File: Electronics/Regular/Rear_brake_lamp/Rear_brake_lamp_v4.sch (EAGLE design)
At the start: 8 parts, among them X2 JST-XH-02-PIN-LONG-PAD

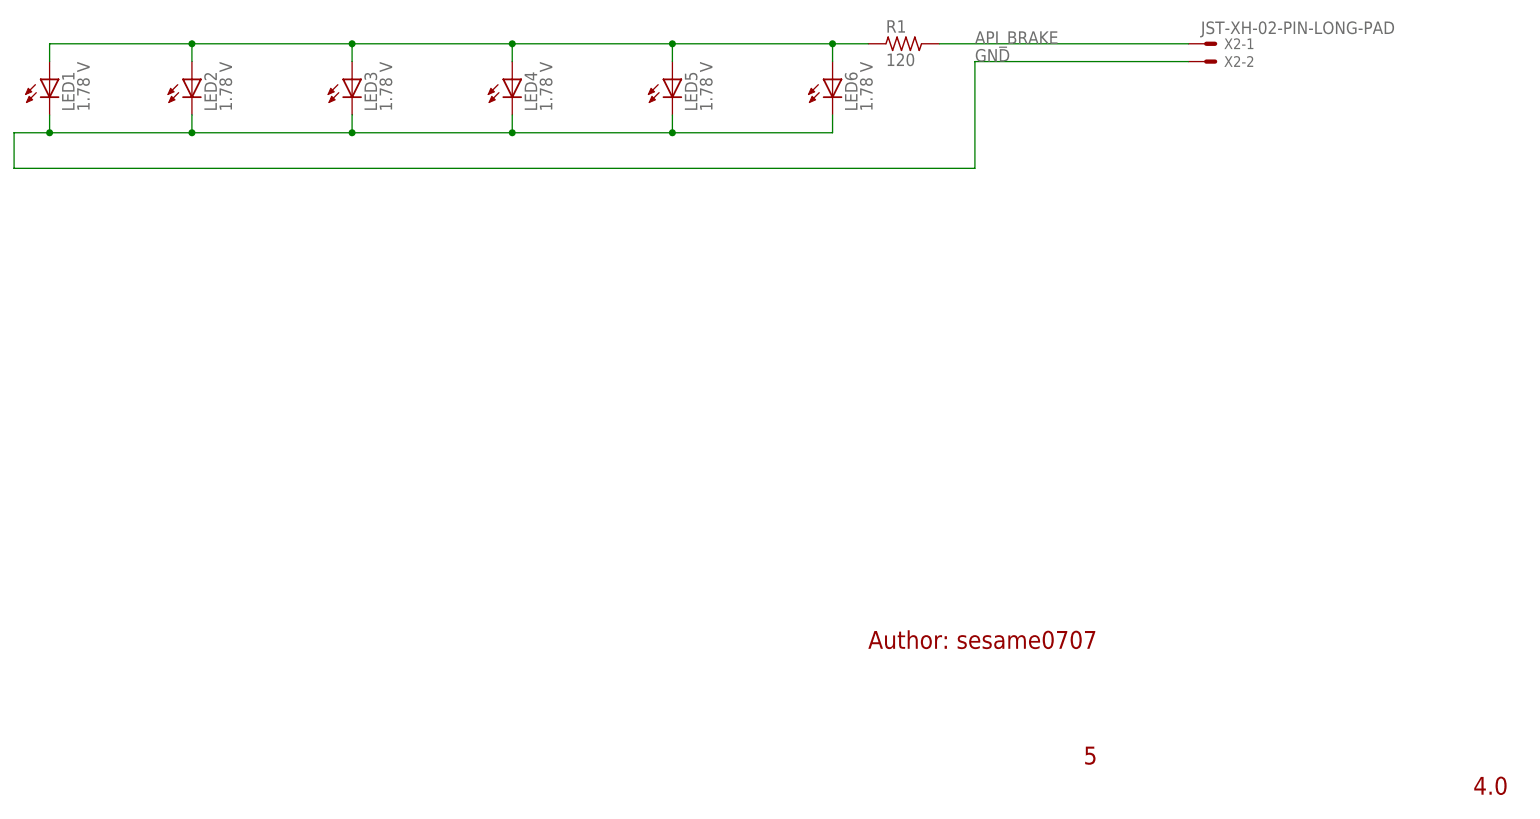
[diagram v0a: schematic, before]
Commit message: BOM on all the lamps added
Note: Version of lamps' projects has increased from x.0 to x.1.

What also has been done:
- some visual refactoring on schematics
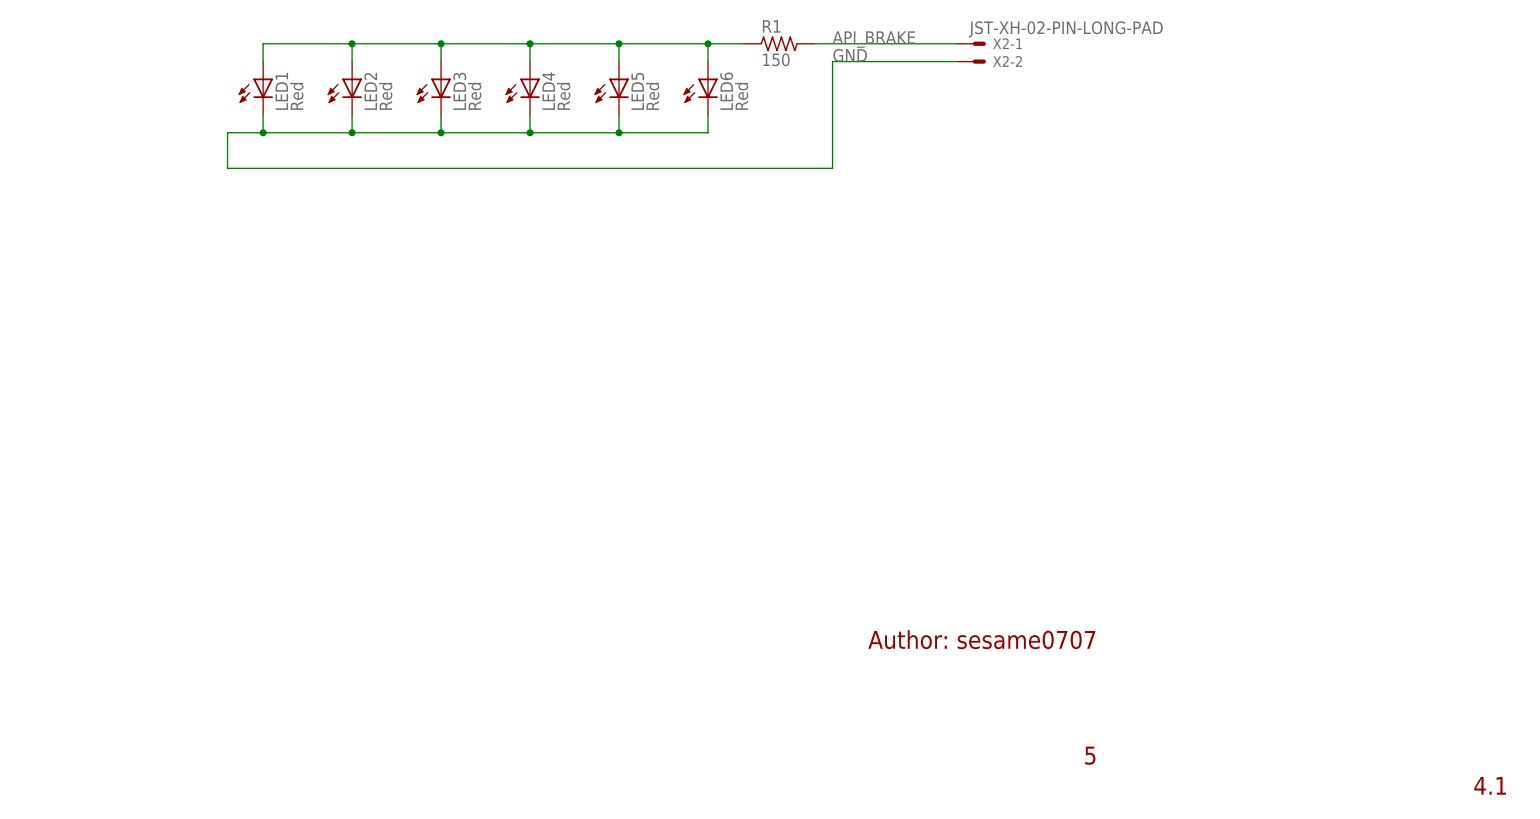
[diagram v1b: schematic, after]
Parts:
- LED1, LED2, LED3, LED4, LED5, LED6: value 1.78 V -> Red; CURRENT 0.32 mA -> (none); CURRENT_EMPIRICAL (none) -> 1.48 mA; MANUFACTURER (none) -> LUCKYLIGHT; MANUFACTURER_PART_NUMBER (none) -> LL-503VD2E-1B; SUPPLIER (none) -> TME; SUPPLIER_PART_NUMBER (none) -> LL-503VD2E-1B; SUPPLIER_URL (none) -> https://www.tme.eu/pl/details/ll-503vd2e-1b/diody-led-tht-o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; VOLTAGE_EMPIRICAL (none) -> 1.83 V
- R1: value 120 -> 150; MANUFACTURER (none) -> ROYAL OHM; MANUFACTURER_PART_NUMBER (none) -> 1206S4J0151T5E; RESISTANCE (none) -> 150 Ohm; SUPPLIER (none) -> TME; SUPPLIER_PART_NUMBER (none) -> 1206S4J0151T5E; SUPPLIER_URL (none) -> https://www.tme.eu/pl/details/1206s4j0151t5e/rezystory-smd/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
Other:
- note added: "4.1"
- note removed: "4.0"
- moved on the sheet: LED1, LED2, LED3, LED4, LED5, LED6, R1, X2-1, X2-2
